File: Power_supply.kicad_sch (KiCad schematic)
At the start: 51 parts, among them J20 HV_Transformer, J21 LV_Transformer, J22 220V, J23 Transformers, J24 Thyratrone, J25 Anodes_enable, J26 Conn_01x04, J27 Conn_01x04, J28 Conn_01x04, K2 SANYOU_SRD_Form_C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

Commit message: Multiple PCB
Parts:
- C24: footprint spdf1626_lib:C_THT_K73-17_P9.00mm -> spdf1626_lib:C_THT_K73-17_P15.00mm
- D12, D13, D14, D15, D20: footprint Diode_THT:D_DO-41_SOD81_P12.70mm_Horizontal -> spdf1626_lib:D_DO-41
- D16, D17, D18, D19: footprint Diode_THT:D_DO-27_P15.24mm_Horizontal -> spdf1626_lib:D_DO-27_P16mm_Horizontal
- J22: footprint Connector_Phoenix_MC_HighVoltage:PhoenixContact_MCV_1,5_2-G-5.08_1x02_P5.08mm_Vertical -> spdf1626_lib:Connector_1x02_P5mm_Vertical
- J25: footprint Connector_Phoenix_MC_HighVoltage:PhoenixContact_MCV_1,5_2-G-5.08_1x02_P5.08mm_Vertical -> spdf1626_lib:PinHeader_1x02_P2.54mm
- L2: footprint spdf1626_lib:L_THT_PLA10 -> spdf1626_lib:L_THT_B82731-T

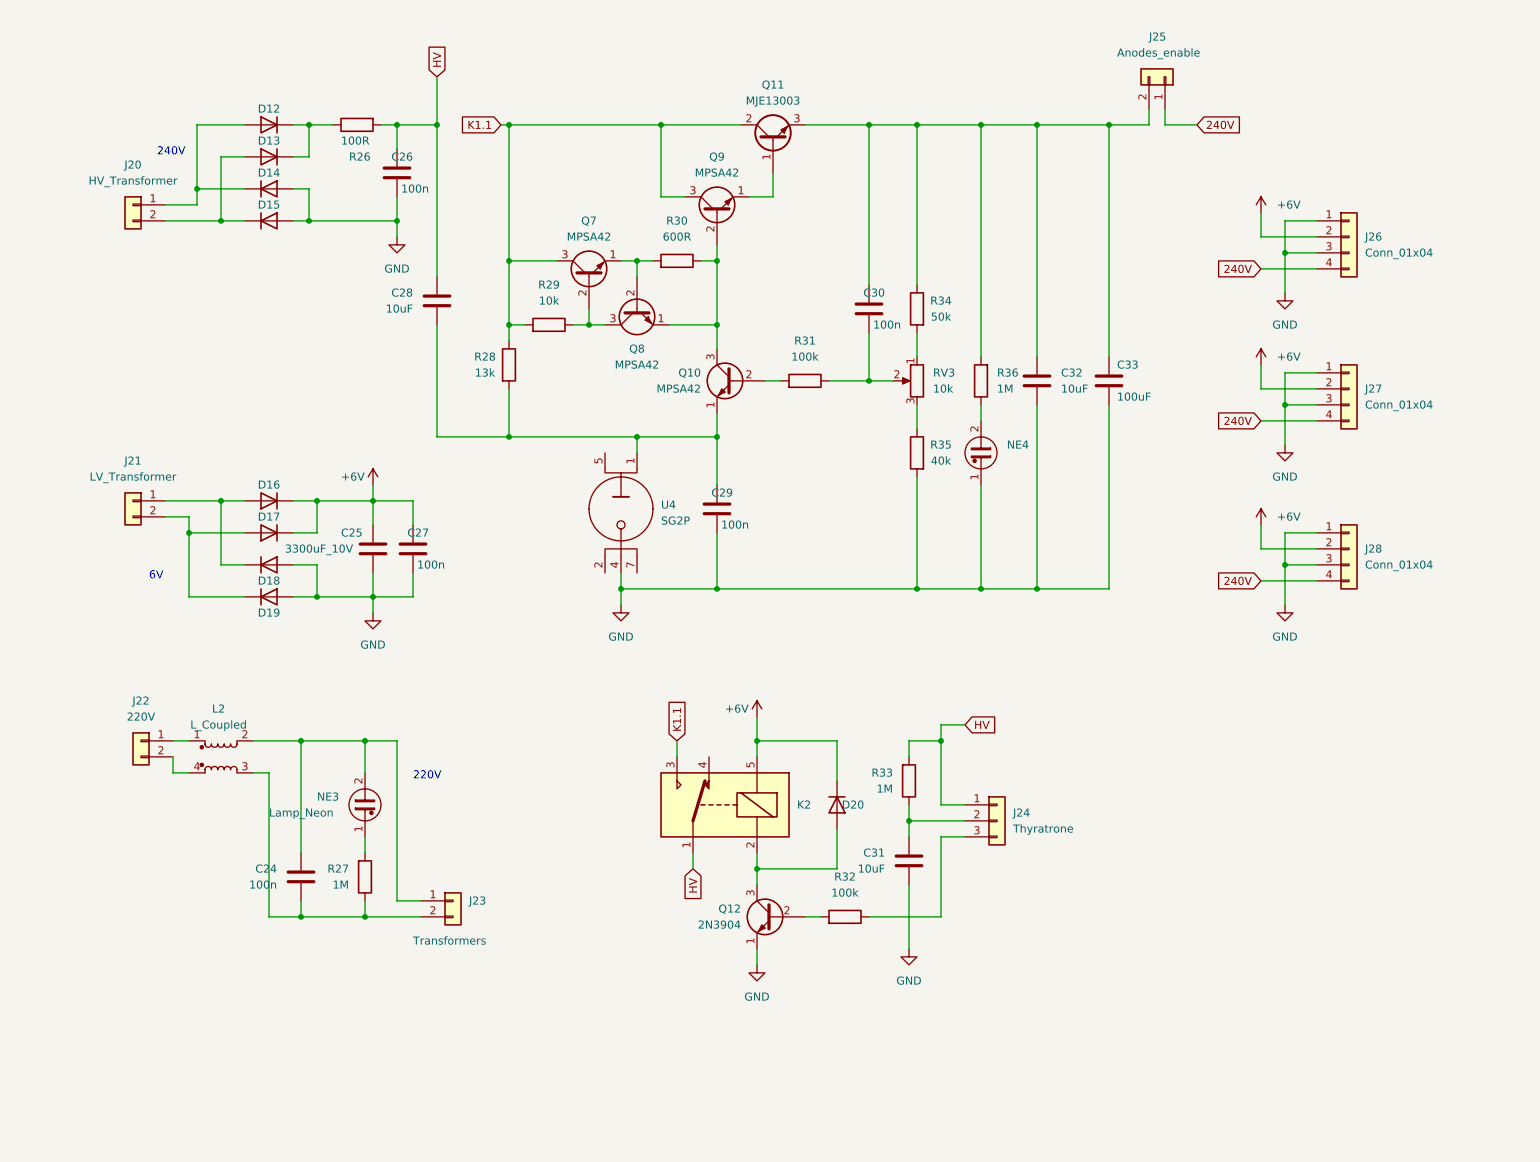
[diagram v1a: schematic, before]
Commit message: New power supply
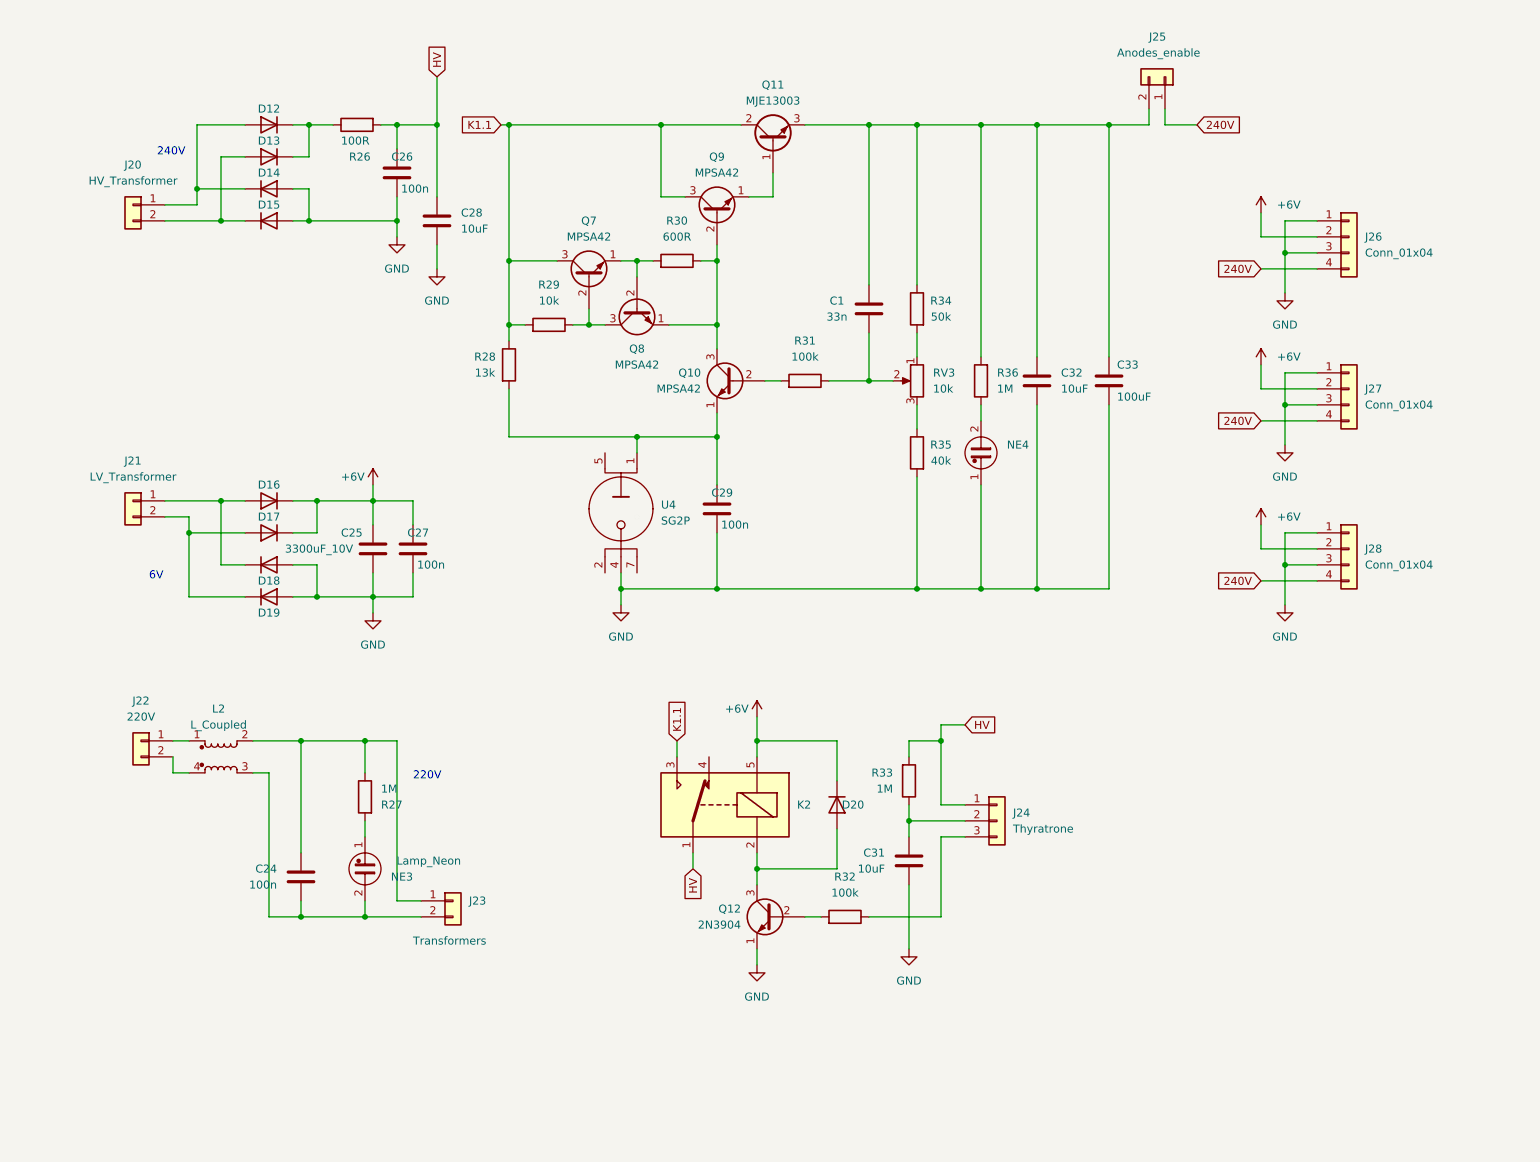
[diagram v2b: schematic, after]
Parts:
- removed C30: 100n, spdf1626_lib:C_THT_K73-17_P9.00mm, symbol Device:C
- added C1: 33n, Capacitor_THT:C_Rect_L7.2mm_W3.0mm_P5.00mm_FKS2_FKP2_MKS2_MKP2, symbol Device:C
- Q11: footprint Package_TO_SOT_THT:TO-126-3_Vertical -> spdf1626_lib:TO-220_Vertical
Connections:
- net GND: now also C28.2
- net at C29.2, Q10.1 (E), R28.2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: no longer C28.2
- net at R31.1, RV3.2: now also C1.1
- net at C32.1, C33.1, J25.2 (Pin_2)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: now also C1.2
- net at C24.1, J23.2 (Pin_2), L2.3: now also NE3.2; no longer R27.1
- net at C24.2, J23.1 (Pin_1), L2.2: now also R27.1; no longer NE3.2
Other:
- moved on the sheet: C28, NE3, R27
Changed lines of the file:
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@@
   (junction (at 193.04 30.48) (diameter 0) (color 0 0 0 0)
   )
-  (junction (at 97.79 80.01) (diameter 0) (color 0 0 0 0)
-  )
   (junction (at 130.81 80.01) (diameter 0) (color 0 0 0 0)
   )
@@
     (stroke (width 0) (type default) (color 0 0 0 0))
   )
-  (wire (pts (xy 74.93 143.51) (xy 74.93 146.05))
+  (wire (pts (xy 74.93 143.51) (xy 74.93 140.97))
     (stroke (width 0) (type default) (color 0 0 0 0))
   )
@@
     (stroke (width 0) (type default) (color 0 0 0 0))
   )
-  (wire (pts (xy 86.36 80.01) (xy 97.79 80.01))
-    (stroke (width 0) (type default) (color 0 0 0 0))
-  )
   (wire (pts (xy 193.04 104.14) (xy 181.61 104.14))
     (stroke (width 0) (type default) (color 0 0 0 0))
@@
     (stroke (width 0) (type default) (color 0 0 0 0))
   )
-  (wire (pts (xy 86.36 62.23) (xy 86.36 80.01))
+  (wire (pts (xy 86.36 49.53) (xy 86.36 53.34))
     (stroke (width 0) (type default) (color 0 0 0 0))
   )
@@
     (stroke (width 0) (type default) (color 0 0 0 0))
   )
-  (wire (pts (xy 86.36 30.48) (xy 86.36 54.61))
+  (wire (pts (xy 86.36 30.48) (xy 86.36 41.91))
     (stroke (width 0) (type default) (color 0 0 0 0))
   )
@@
     (pin "3")
   )
+  (symbol (lib_id "power:GND") (at 86.36 53.34 0) (unit 1)
+    (in_bom yes) (on_board yes) (fields_autoplaced)
+    (property "Reference" "#PWR0101" (id 0) (at 86.36 59.69 0)
+      (effects (font (size 1.27 1.27)) hide)
+    )
+    (property "Value" "GND" (id 1) (at 86.36 58.42 0))
+    (property "Footprint" "" (id 2) (at 86.36 53.34 0)
+      (effects (font (size 1.27 1.27)) hide)
+    )
+    (property "Datasheet" "" (id 3) (at 86.36 53.34 0)
+      (effects (font (size 1.27 1.27)) hide)
+    )
+    (pin "1")
+  )
   (symbol (lib_id "Connector_Generic:Conn_01x04") (at 231.14 48.26 0) (unit 1)
     (in_bom yes) (on_board yes) (fields_autoplaced)
@@
     (pin "2")
   )
-  (symbol (lib_id "Device:C") (at 154.94 59.69 0) (mirror x) (unit 1)
-    (in_bom yes) (on_board yes)
-    (property "Reference" "C30" (id 0) (at 157.48 57.15 0)
-      (effects (font (size 1.27 1.27)) (justify right))
-    )
-    (property "Value" "100n" (id 1) (at 160.02 62.23 0)
-      (effects (font (size 1.27 1.27)) (justify right))
-    )
-    (property "Footprint" "spdf1626_lib:C_THT_K73-17_P9.00mm" (id 2) (at 155.9052 55.88 0)
-      (effects (font (size 1.27 1.27)) hide)
-    )
-    (property "Datasheet" "~" (id 3) (at 154.94 59.69 0)
-      (effects (font (size 1.27 1.27)) hide)
-    )
-    (pin "1")
-    (pin "2")
-  )
   (symbol (lib_id "Transistor_BJT:MJE13003") (at 139.7 33.02 90) (unit 1)
     (in_bom yes) (on_board yes) (fields_autoplaced)
     (property "Reference" "Q11" (id 0) (at 139.7 24.13 90))
     (property "Value" "MJE13003" (id 1) (at 139.7 26.67 90))
-    (property "Footprint" "Package_TO_SOT_THT:TO-126-3_Vertical" (id 2) (at 141.605 27.94 0)
+    (property "Footprint" "spdf1626_lib:TO-220_Vertical" (id 2) (at 141.605 27.94 0)
       (effects (font (size 1.27 1.27) italic) (justify left) hide)
     )
@@
     (pin "4")
   )
-  (symbol (lib_id "Device:C") (at 86.36 58.42 0) (mirror y) (unit 1)
-    (in_bom yes) (on_board yes)
-    (property "Reference" "C28" (id 0) (at 82.55 57.1499 0)
-      (effects (font (size 1.27 1.27)) (justify left))
-    )
-    (property "Value" "10uF" (id 1) (at 82.55 59.6899 0)
-      (effects (font (size 1.27 1.27)) (justify left))
-    )
-    (property "Footprint" "spdf1626_lib:C_THT_D10.0mm_P5.00mm" (id 2) (at 85.3948 62.23 0)
-      (effects (font (size 1.27 1.27)) hide)
-    )
-    (property "Datasheet" "~" (id 3) (at 86.36 58.42 0)
+  (symbol (lib_id "Device:C") (at 86.36 45.72 0) (unit 1)
+    (in_bom yes) (on_board yes)
+    (property "Reference" "C28" (id 0) (at 90.17 44.4499 0)
+      (effects (font (size 1.27 1.27)) (justify left))
+    )
+    (property "Value" "10uF" (id 1) (at 90.17 46.9899 0)
+      (effects (font (size 1.27 1.27)) (justify left))
+    )
+    (property "Footprint" "spdf1626_lib:C_THT_D10.0mm_P5.00mm" (id 2) (at 87.3252 49.53 0)
+      (effects (font (size 1.27 1.27)) hide)
+    )
+    (property "Datasheet" "~" (id 3) (at 86.36 45.72 0)
       (effects (font (size 1.27 1.27)) hide)
     )
@@
     (pin "2")
   )
-  (symbol (lib_id "Device:R") (at 74.93 149.86 0) (mirror x) (unit 1)
-    (in_bom yes) (on_board yes) (fields_autoplaced)
-    (property "Reference" "R27" (id 0) (at 72.39 148.5899 0)
+  (symbol (lib_id "Device:R") (at 74.93 137.16 0) (mirror y) (unit 1)
+    (in_bom yes) (on_board yes) (fields_autoplaced)
+    (property "Reference" "R27" (id 0) (at 77.47 138.4301 0)
       (effects (font (size 1.27 1.27)) (justify right))
     )
-    (property "Value" "1M" (id 1) (at 72.39 151.1299 0)
+    (property "Value" "1M" (id 1) (at 77.47 135.8901 0)
       (effects (font (size 1.27 1.27)) (justify right))
     )
-    (property "Footprint" "spdf1626_lib:R_THT_025W" (id 2) (at 73.152 149.86 90)
-      (effects (font (size 1.27 1.27)) hide)
-    )
-    (property "Datasheet" "~" (id 3) (at 74.93 149.86 0)
+    (property "Footprint" "spdf1626_lib:R_THT_025W" (id 2) (at 76.708 137.16 90)
+      (effects (font (size 1.27 1.27)) hide)
+    )
+    (property "Datasheet" "~" (id 3) (at 74.93 137.16 0)
       (effects (font (size 1.27 1.27)) hide)
     )
@@
     (pin "3")
   )
+  (symbol (lib_id "Device:C") (at 154.94 59.69 0) (mirror x) (unit 1)
+    (in_bom yes) (on_board yes)
+    (property "Reference" "C1" (id 0) (at 149.86 58.42 0))
+    (property "Value" "33n" (id 1) (at 149.86 60.96 0))
+    (property "Footprint" "Capacitor_THT:C_Rect_L7.2mm_W3.0mm_P5.00mm_FKS2_FKP2_MKS2_MKP2" (id 2) (at 155.9052 55.88 0)
+      (effects (font (size 1.27 1.27)) hide)
+    )
+    (property "Datasheet" "~" (id 3) (at 154.94 59.69 0)
+      (effects (font (size 1.27 1.27)) hide)
+    )
+    (pin "1")
+    (pin "2")
+  )
   (symbol (lib_id "power:GND") (at 220.98 57.15 0) (unit 1)
     (in_bom yes) (on_board yes) (fields_autoplaced)
@@
     (pin "1")
   )
-  (symbol (lib_id "Device:Lamp_Neon") (at 74.93 138.43 0) (unit 1)
-    (in_bom yes) (on_board yes)
-    (property "Reference" "NE3" (id 0) (at 67.31 137.16 0)
-      (effects (font (size 1.27 1.27)) (justify left))
-    )
-    (property "Value" "Lamp_Neon" (id 1) (at 59.69 139.7 0)
-      (effects (font (size 1.27 1.27)) (justify left))
-    )
-    (property "Footprint" "spdf1626_lib:PinHeader_1x02_P2.54mm" (id 2) (at 74.93 135.89 90)
-      (effects (font (size 1.27 1.27)) hide)
-    )
-    (property "Datasheet" "~" (id 3) (at 74.93 135.89 90)
+  (symbol (lib_id "Device:Lamp_Neon") (at 74.93 148.59 180) (unit 1)
+    (in_bom yes) (on_board yes)
+    (property "Reference" "NE3" (id 0) (at 82.55 149.86 0)
+      (effects (font (size 1.27 1.27)) (justify left))
+    )
+    (property "Value" "Lamp_Neon" (id 1) (at 90.17 147.32 0)
+      (effects (font (size 1.27 1.27)) (justify left))
+    )
+    (property "Footprint" "spdf1626_lib:PinHeader_1x02_P2.54mm" (id 2) (at 74.93 151.13 90)
+      (effects (font (size 1.27 1.27)) hide)
+    )
+    (property "Datasheet" "~" (id 3) (at 74.93 151.13 90)
       (effects (font (size 1.27 1.27)) hide)
     )
@@
       (reference "#PWR048") (unit 1) (value "GND") (footprint "")
     )
+    (path "/18b770dc-28cc-4a8f-a017-c303931d7c49"
+      (reference "#PWR0101") (unit 1) (value "GND") (footprint "")
+    )
+    (path "/cac9add8-7e11-41d7-b5dc-f00d79bea5c0"
+      (reference "C1") (unit 1) (value "33n") (footprint "Capacitor_THT:C_Rect_L7.2mm_W3.0mm_P5.00mm_FKS2_FKP2_MKS2_MKP2")
+    )
     (path "/5d968c0b-27b9-4fe9-9728-a935b5d5967c"
       (reference "C24") (unit 1) (value "100n") (footprint "spdf1626_lib:C_THT_K73-17_P15.00mm")
@@
       (reference "C29") (unit 1) (value "100n") (footprint "spdf1626_lib:C_THT_K73-17_P9.00mm")
     )
-    (path "/1e7925bf-34d5-4616-a67e-03802af9f0a1"
-      (reference "C30") (unit 1) (value "100n") (footprint "spdf1626_lib:C_THT_K73-17_P9.00mm")
-    )
     (path "/1b7251c7-d2e0-472d-afcc-5272cac6a377"
       (reference "C31") (unit 1) (value "10uF") (footprint "spdf1626_lib:C_THT_D10.0mm_P5.00mm")
@@
     )
     (path "/1f28c394-5583-4c54-aeca-6f975fc7fa47"
-      (reference "Q11") (unit 1) (value "MJE13003") (footprint "Package_TO_SOT_THT:TO-126-3_Vertical")
+      (reference "Q11") (unit 1) (value "MJE13003") (footprint "spdf1626_lib:TO-220_Vertical")
     )
     (path "/671e6eb7-fa05-4f91-b6c4-a9fb84d7ecfa"

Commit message: New power supply schematic
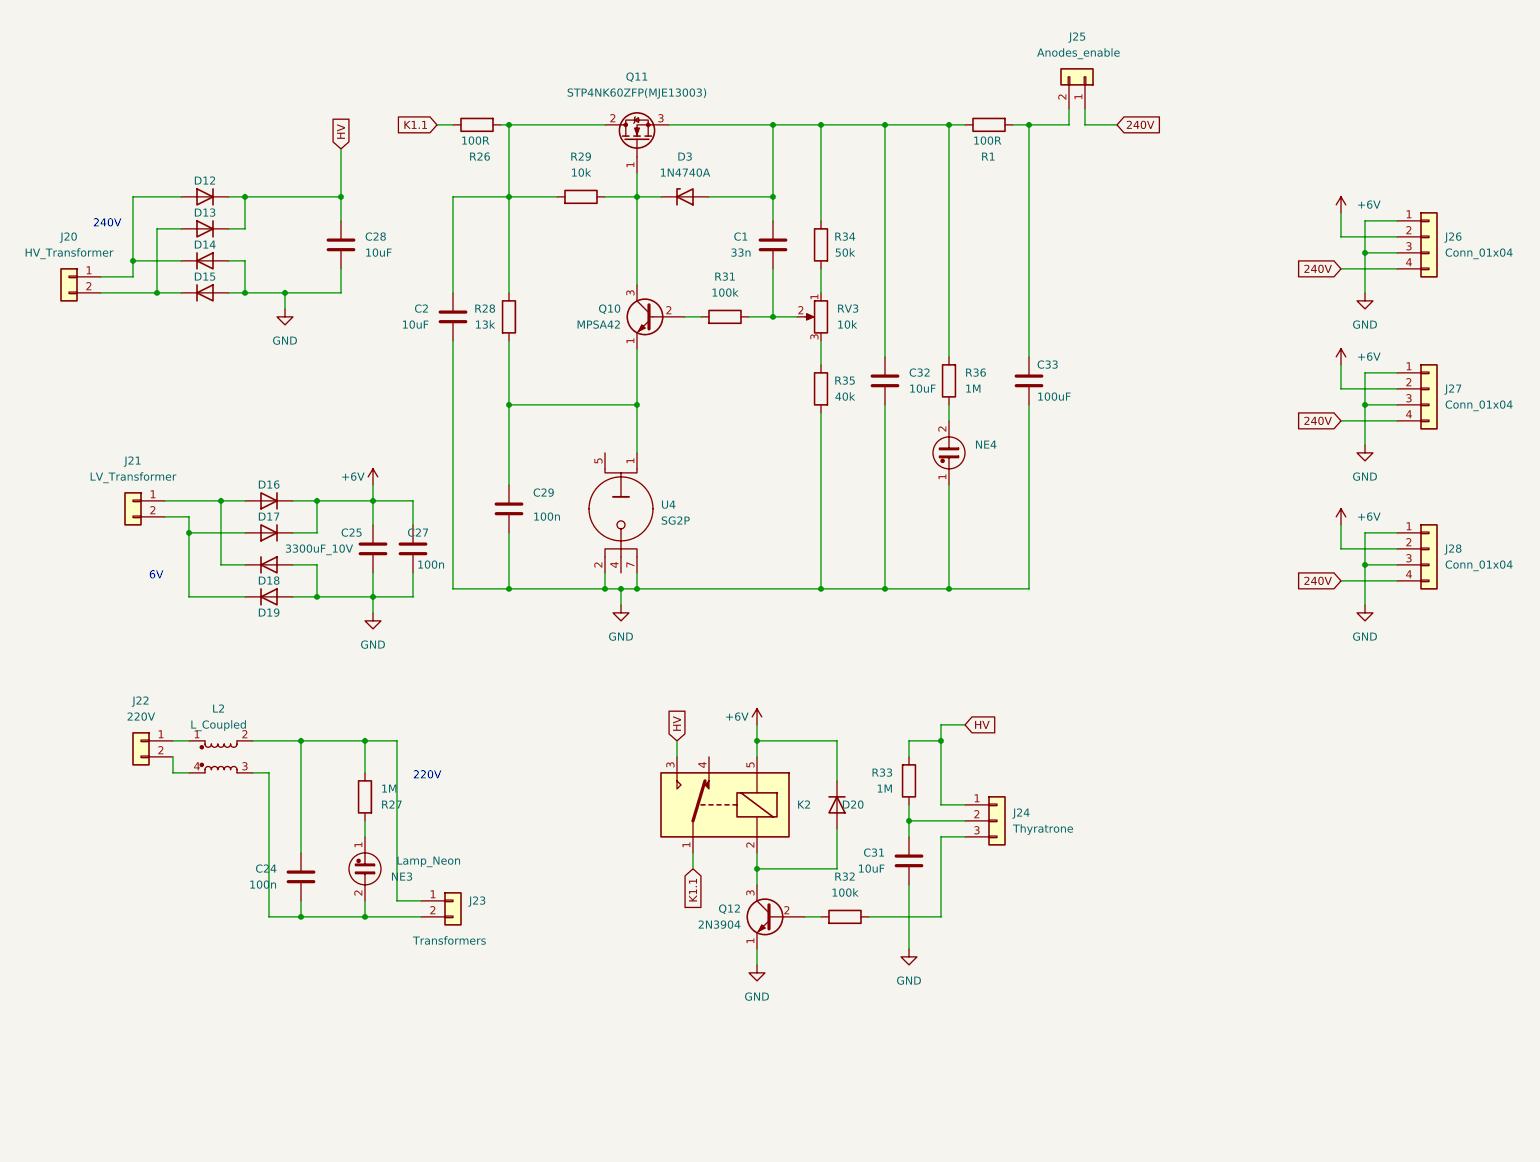
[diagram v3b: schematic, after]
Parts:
- removed C26: 100n, spdf1626_lib:C_THT_K73-17_P9.00mm, symbol Device:C
- removed Q11: MJE13003, spdf1626_lib:TO-220_Vertical, symbol Transistor_BJT:MJE13003
- removed Q7, Q8, Q9: MPSA42, Package_TO_SOT_THT:TO-92_Inline, symbol Transistor_BJT:MPSA42
- removed R30: 600R, spdf1626_lib:R_THT_025W, symbol Device:R
- added C2: 10uF, spdf1626_lib:C_THT_D10.0mm_P5.00mm, symbol Device:C
- added D3: 1N4740A, spdf1626_lib:D_DO-41, symbol Diode:1N47xxA
- added Q11: STP4NK60ZFP(MJE13003), spdf1626_lib:TO-220-3_Vertical, symbol Transistor_FET:IRF740
- added R1: 100R, spdf1626_lib:R_THT_1W, symbol Device:R
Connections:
- net GND: now also U4.2, U4.7, C2.2; no longer U4.4
- net HV: now also D12.1 (K), D13.1 (K), K2.3; no longer K2.1, R26.2
- net K1.1: now also K2.1, R26.1; no longer K2.3, R28.1, R29.2
- net at Q10.3 (C): now also R29.1, D3.1 (K), Q11.1 (G)
- net at C1.2, C32.1, R34.1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: now also D3.2 (A), Q11.3 (S), R1.1; no longer C33.1, J25.2 (Pin_2)
- new net: C2.1, Q11.2 (D), R26.2, R28.1, R29.2
- new net: C33.1, J25.2 (Pin_2), R1.2
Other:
- moved on the sheet: C1, C28, C29, C32, C33, D12, D13, D14, D15, J20, J25, J26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

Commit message: New power supply PCB
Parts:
- added D1: BZX55C75, spdf1626_lib:D_THT_DO-35_SOD27_Horizontal, symbol Diode:1N47xxA
- added J1: Transformers, spdf1626_lib:Connector_1x02_P5mm_Vertical, symbol Connector_Generic:Conn_01x02
- J23: footprint spdf1626_lib:PinHeader_1x02_P2.54mm -> spdf1626_lib:Connector_1x02_P5mm_Vertical
- R28: footprint spdf1626_lib:R_THT_025W -> spdf1626_lib:R_THT_1W
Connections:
- net HV: now also D1.1 (K); no longer J24.1 (Pin_1)
- net at C24.1, J23.2 (Pin_2), L2.3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: now also J1.2 (Pin_2)
- net at C24.2, J23.1 (Pin_1), L2.2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: now also J1.1 (Pin_1)
- new net: D1.2 (A), J24.1 (Pin_1)
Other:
- moved on the sheet: J23, NE3
